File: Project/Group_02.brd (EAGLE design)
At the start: 71.1 x 44.5 mm, 29 parts, among them J1 POWER_JACKPTH_LOCK, U1 +12v

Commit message: Completamento board
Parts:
- moved C2 0.63 mm to (5.08, 38.7)
- moved C3 0.33 mm to (5.08, 35.2)
- moved J3 0.06 mm to (51.5, 31.1)
- moved J4 0.06 mm to (51.5, 36.7)
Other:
- board text added: "0.1μF"
- board text added: "0.33μF"
- board text added: "10K"
- board text added: "5V"
- board text added: "BOARD"
- board text added: "CY8CKIT059-TARGET"
- board text added: "D1 BLUE"
- board text added: "GND"
- board text added: "GROUP 02"
- board text added: "MUX PINS"
- board text added: "POWER JACK CONNECTOR"
- board text added: "PTC"
- board text added: "S1"
- board text added: "TCA 9546A"
- board text added: "TMP"
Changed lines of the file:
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@@
 <dimension x1="-1.27" y1="0" x2="-1.27" y2="44.45" x3="-2.54" y3="22.225" textsize="1.778" layer="51"/>
 <dimension x1="0" y1="46.99" x2="71.12" y2="46.99" x3="35.56" y3="45.72" textsize="1.778" layer="51"/>
-<hole x="3.175" y="42.291" drill="2.5"/>
-<hole x="3.175" y="2.032" drill="2.5"/>
-<hole x="68.58" y="2.032" drill="2.5"/>
-<hole x="68.58" y="42.291" drill="2.5"/>
+<hole x="3.175" y="42.291" drill="3"/>
+<hole x="3.175" y="1.905" drill="3"/>
+<hole x="68.58" y="1.905" drill="3"/>
+<hole x="68.58" y="42.291" drill="3"/>
+<text x="54.483" y="8.382" size="1.016" layer="21">CY8CKIT059-TARGET</text>
+<text x="39.116" y="33.147" size="0.8128" layer="21">TCA
+9546A</text>
+<text x="68.961" y="30.607" size="0.8128" layer="21" rot="R90">POWER JACK
+CONNECTOR</text>
+<text x="5.588" y="0.889" size="0.8128" layer="21">D1 BLUE</text>
+<text x="5.207" y="27.813" size="0.8128" layer="21">GND</text>
+<text x="3.175" y="27.813" size="0.8128" layer="21">5V</text>
+<wire x1="8.89" y1="25.4" x2="8.89" y2="24.13" width="0.1524" layer="21"/>
+<wire x1="8.89" y1="24.13" x2="11.43" y2="24.13" width="0.1524" layer="21"/>
+<wire x1="11.43" y1="24.13" x2="13.97" y2="24.13" width="0.1524" layer="21"/>
+<wire x1="13.97" y1="24.13" x2="16.51" y2="24.13" width="0.1524" layer="21"/>
+<wire x1="16.51" y1="24.13" x2="16.51" y2="25.4" width="0.1524" layer="21"/>
+<text x="9.906" y="22.86" size="0.8128" layer="21">MUX PINS</text>
+<wire x1="11.43" y1="25.4" x2="11.43" y2="24.13" width="0.1524" layer="21"/>
+<wire x1="13.97" y1="25.4" x2="13.97" y2="24.13" width="0.1524" layer="21"/>
+<text x="63.627" y="4.318" size="0.8128" layer="21">GND</text>
+<text x="66.802" y="4.318" size="0.8128" layer="21">5V</text>
+<text x="36.703" y="39.497" size="0.6096" layer="21">0.33μF</text>
+<text x="2.032" y="37.719" size="0.6096" layer="21" rot="R90">0.1μF</text>
+<text x="2.032" y="34.29" size="0.6096" layer="21" rot="R90">0.1μF</text>
+<text x="11.557" y="37.338" size="0.6096" layer="21">PTC</text>
+<text x="25.146" y="38.608" size="0.8128" layer="21">TMP</text>
+<text x="13.462" y="42.037" size="1.016" layer="21">S1</text>
+<text x="24.257" y="1.27" size="0.6096" layer="21">10K</text>
+<text x="57.15" y="42.164" size="1.27" layer="21">GROUP 02</text>
+<text x="59.69" y="40.513" size="1.27" layer="21">BOARD</text>
 </plain>
 <attributes>
@@
 <attribute name="VALUE" x="37.211" y="39.751" size="0.6096" layer="27" font="vector" ratio="20" rot="R270" align="top-center"/>
 </element>
-<element name="C2" library="SparkFun-Capacitors" package="CAP-PTH-SMALL-KIT" value="0.1uF" x="5.08" y="39.37" smashed="yes" rot="R180">
-<attribute name="PROD_ID" value="CAP-08370" x="-34.29" y="95.25" size="1.778" layer="27" rot="R180" display="off"/>
-</element>
-<element name="C3" library="SparkFun-Capacitors" package="CAP-PTH-SMALL-KIT" value="0.1uF" x="5.08" y="35.56" smashed="yes" rot="R180">
-<attribute name="PROD_ID" value="CAP-08370" x="-40.64" y="91.44" size="1.778" layer="27" rot="R180" display="off"/>
+<element name="C2" library="SparkFun-Capacitors" package="CAP-PTH-SMALL-KIT" value="0.1uF" x="5.08" y="38.735" smashed="yes" rot="R180">
+<attribute name="PROD_ID" value="CAP-08370" x="-34.29" y="94.615" size="1.778" layer="27" rot="R180" display="off"/>
+</element>
+<element name="C3" library="SparkFun-Capacitors" package="CAP-PTH-SMALL-KIT" value="0.1uF" x="5.08" y="35.2298" smashed="yes" rot="R180">
+<attribute name="PROD_ID" value="CAP-08370" x="-40.64" y="91.1098" size="1.778" layer="27" rot="R180" display="off"/>
 </element>
 <element name="D1" library="SparkFun-LED" package="LED-1206" value="BLUE" x="7.62" y="2.54" smashed="yes">
@@
 <attribute name="VALUE" x="2.54" y="29.718" size="0.6096" layer="27" font="vector" ratio="20"/>
 </element>
-<element name="J3" library="SparkFun-Connectors" package="1X02" value="" x="51.562" y="31.115" smashed="yes" rot="R90">
-<attribute name="NAME" x="50.165" y="29.845" size="0.6096" layer="25" font="vector" ratio="20" rot="R90"/>
-<attribute name="VALUE" x="53.594" y="29.845" size="0.6096" layer="27" font="vector" ratio="20" rot="R90"/>
-</element>
-<element name="J4" library="SparkFun-Connectors" package="1X02" value="" x="51.435" y="36.703" smashed="yes" rot="R90">
-<attribute name="NAME" x="50.038" y="35.433" size="0.6096" layer="25" font="vector" ratio="20" rot="R90"/>
-<attribute name="VALUE" x="53.467" y="35.433" size="0.6096" layer="27" font="vector" ratio="20" rot="R90"/>
+<element name="J3" library="SparkFun-Connectors" package="1X02" value="" x="51.4985" y="31.115" smashed="yes" rot="R90">
+<attribute name="NAME" x="50.1015" y="29.845" size="0.6096" layer="25" font="vector" ratio="20" rot="R90"/>
+<attribute name="VALUE" x="53.5305" y="29.845" size="0.6096" layer="27" font="vector" ratio="20" rot="R90"/>
+</element>
+<element name="J4" library="SparkFun-Connectors" package="1X02" value="" x="51.4985" y="36.703" smashed="yes" rot="R90">
+<attribute name="NAME" x="50.1015" y="35.433" size="0.6096" layer="25" font="vector" ratio="20" rot="R90"/>
+<attribute name="VALUE" x="53.5305" y="35.433" size="0.6096" layer="27" font="vector" ratio="20" rot="R90"/>
 </element>
 <element name="J5" library="SparkFun-Connectors" package="1X02" value="" x="33.655" y="38.862" smashed="yes" rot="R180">
@@
 <contactref element="U$1" pad="28"/>
 <contactref element="R11" pad="P$1"/>
-<contactref element="C3" pad="2"/>
-<contactref element="U$3" pad="12"/>
-<contactref element="U$2" pad="8"/>
 <contactref element="U$2" pad="3"/>
 <polygon width="0.2032" layer="1" isolate="0.3048">
@@
 <wire x1="24.892" y1="36.703" x2="24.257" y2="36.703" width="0.254" layer="1"/>
 <wire x1="24.257" y1="36.703" x2="22.86" y2="38.1" width="0.254" layer="1"/>
-<wire x1="22.86" y1="38.1" x2="21.409" y2="38.1" width="0.254" layer="1"/>
-<wire x1="21.409" y1="38.1" x2="20.104" y2="36.795" width="0.254" layer="1"/>
+<wire x1="22.86" y1="38.1" x2="21.59" y2="38.1" width="0.254" layer="1"/>
+<contactref element="U$3" pad="12"/>
+<contactref element="C3" pad="2"/>
+<contactref element="U$2" pad="8"/>
+<wire x1="21.59" y1="38.1" x2="21.409" y2="38.1" width="0.254" layer="1"/>
+<wire x1="20.104" y1="36.795" x2="21.409" y2="38.1" width="0.254" layer="1"/>
 </signal>
 <signal name="12V">
@@
 <via x="46.609" y="34.036" extent="1-16" drill="0.35"/>
 <wire x1="46.609" y1="34.036" x2="49.276" y2="36.703" width="0.254" layer="16"/>
-<wire x1="49.276" y1="36.703" x2="51.435" y2="36.703" width="0.254" layer="16"/>
+<wire x1="49.276" y1="36.703" x2="51.4985" y2="36.703" width="0.254" layer="16"/>
 <wire x1="44.95013125" y1="34.6938" x2="45.47386875" y2="34.6938" width="0.254" layer="1"/>
 <wire x1="45.47386875" y1="34.6938" x2="45.8442" y2="34.32346875" width="0.254" layer="1"/>
@@
 <contactref element="U$2" pad="7"/>
 <contactref element="R3" pad="1"/>
-<wire x1="51.435" y1="39.243" x2="48.983" y2="36.791" width="0.254" layer="1"/>
-<wire x1="48.983" y1="36.791" x2="48.983" y2="35.56" width="0.254" layer="1"/>
+<wire x1="51.4985" y1="39.243" x2="48.983" y2="36.7275" width="0.254" layer="1"/>
+<wire x1="48.983" y1="36.7275" x2="48.983" y2="35.56" width="0.254" layer="1"/>
 <wire x1="48.983" y1="35.56" x2="48.8192125" y2="35.56" width="0.254" layer="1"/>
 <wire x1="48.8192125" y1="35.56" x2="47.9382125" y2="36.441" width="0.254" layer="1"/>
@@
 <wire x1="43.54" y1="32.695" x2="44.45" y2="32.695" width="0.254" layer="1"/>
 <wire x1="49.149" y1="32.981" x2="51.015" y2="31.115" width="0.254" layer="1"/>
-<wire x1="51.015" y1="31.115" x2="51.562" y2="31.115" width="0.254" layer="1"/>
+<wire x1="51.015" y1="31.115" x2="51.4985" y2="31.115" width="0.254" layer="1"/>
 <wire x1="44.45" y1="32.695" x2="44.56086875" y2="32.695" width="0.254" layer="1"/>
 <wire x1="44.56086875" y1="32.695" x2="45.10426875" y2="32.1516" width="0.254" layer="1"/>
@@
 <wire x1="47.498" y1="34.04106875" x2="47.498" y2="32.981" width="0.254" layer="1"/>
 <wire x1="49.7542125" y1="33.912" x2="50.0112125" y2="33.655" width="0.254" layer="1"/>
-<wire x1="50.0112125" y1="33.655" x2="51.562" y2="33.655" width="0.254" layer="1"/>
+<wire x1="50.0112125" y1="33.655" x2="51.4985" y2="33.655" width="0.254" layer="1"/>
 <wire x1="47.498" y1="32.981" x2="48.429" y2="33.912" width="0.254" layer="1"/>
 <wire x1="48.429" y1="33.912" x2="49.7542125" y2="33.912" width="0.254" layer="1"/>
@@
 </board>
 </drawing>
+<compatibility>
+<note version="6.3" minversion="6.2.2" severity="warning">
+Since Version 6.2.2 text objects can contain more than one line,
+which will not be processed correctly with this version.
+</note>
+</compatibility>
 </eagle>

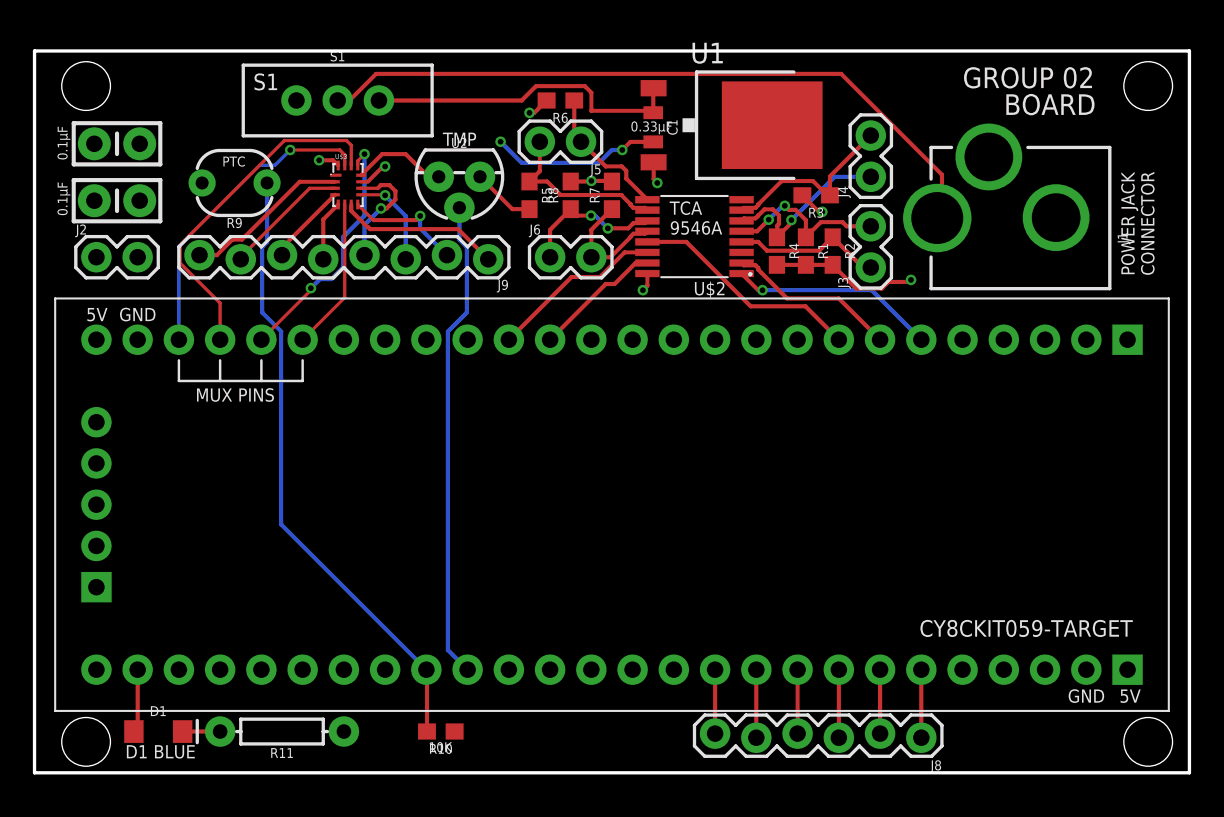
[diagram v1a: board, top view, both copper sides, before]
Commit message: Ottimizzazione dimensioni board
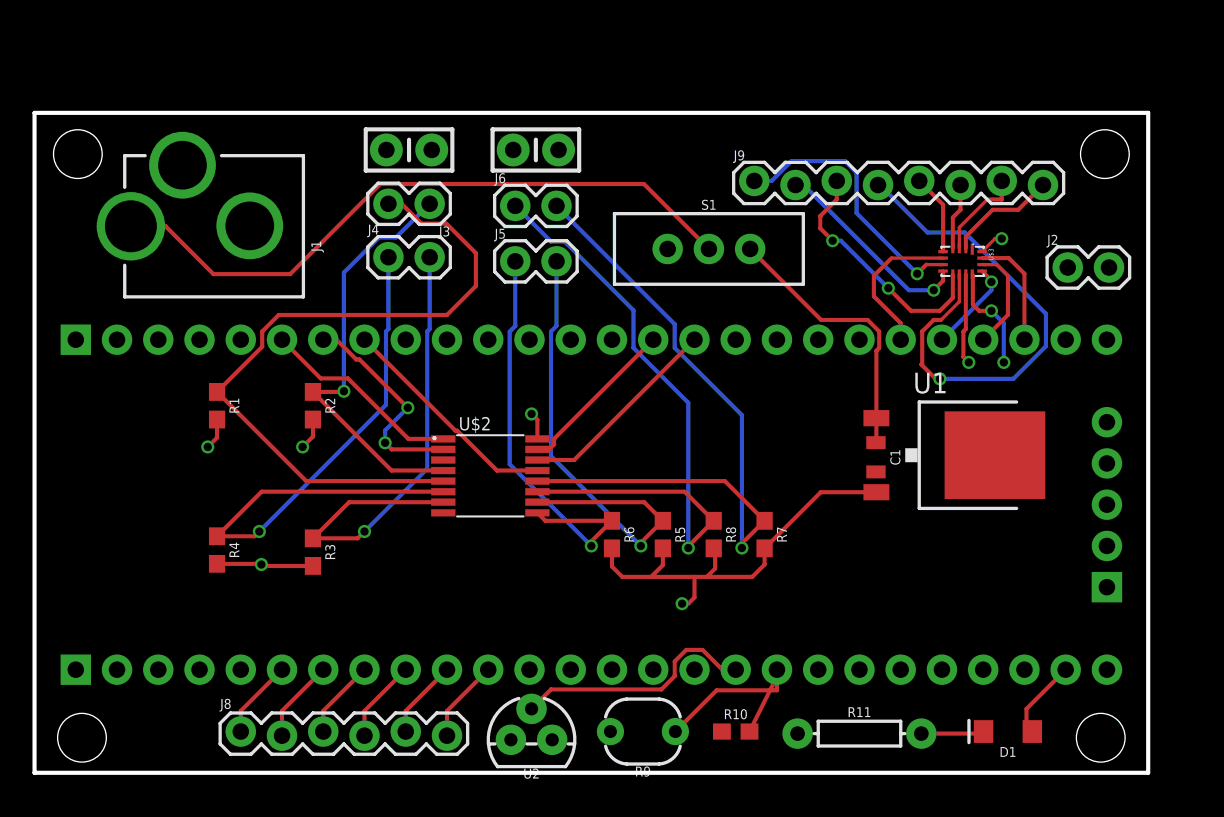
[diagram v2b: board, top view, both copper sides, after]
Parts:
- moved J2 59.8 mm to (63.6, 31.1)
- moved D1 52.3 mm to (59.9, 2.54), turned to 180 degrees
- moved J1 49.7 mm to (19.8, 33.7)
- moved R9 42.1 mm to (37.5, 2.54)
- moved J8 41.9 mm to (12.7, 2.54), turned to 0 degrees
- moved R4 39.1 mm to (11.2, 13.7)
- moved U$3 38.1 mm to (57.1, 31.5), turned to 270 degrees
- moved R3 38.0 mm to (17.1, 13.6), turned to 270 degrees
- moved R1 37.5 mm to (11.2, 22.6)
- moved R11 35.6 mm to (50.8, 2.41), turned to 0 degrees
- moved U2 35.0 mm to (30.6, 2.03), turned to 0 degrees
- moved R2 33.4 mm to (17.1, 22.6)
- moved J4 30.1 mm to (21.8, 31.8), turned to 0 degrees
- moved J3 27.4 mm to (24.3, 35.0), turned to 180 degrees
- moved R6 26.9 mm to (35.6, 14.7), turned to 270 degrees
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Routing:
- net I2C_SCL_3: track 7.62 -> 43.1 mm, vias 0 -> 1
- net I2C_SCL_0: track 10.5 -> 44.1 mm, vias 2 -> 0
- net I2C_SDA_3: track 8.89 -> 39.9 mm, vias 2 -> 1
- net I2C_SDA_1: track 11.5 -> 38.0 mm
- net PHOTO_OUT: track 38.1 -> 12.4 mm
- net N$14: track 7.29 -> 31.3 mm
- net 5V: track 24.2 -> 45.3 mm, vias 8 -> 7
- net I2C_SCL_1: track 11.3 -> 30.8 mm, vias 0 -> 1
- net I2C_SCL_2: track 10.7 -> 30.3 mm, vias 0 -> 1
- net I2C_SDA_2: track 8.55 -> 26.6 mm, vias 0 -> 1
- net I2C_SDA_0: track 9.30 -> 26.3 mm, vias 0 -> 1
- net MUX_A1: track 21.4 -> 6.45 mm
- net TEMP_OUT: track 29.6 -> 15.1 mm
- net MUX_A0: track 19.2 -> 7.07 mm, vias 1 -> 0
- net GND: track 16.4 -> 6.67 mm
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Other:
- board size 71.1 x 44.5 mm -> 68.6 x 40.6 mm
- board text removed: "0.1μF"
- board text removed: "0.33μF"
- board text removed: "10K"
- board text removed: "5V"
- board text removed: "BOARD"
- board text removed: "CY8CKIT059-TARGET"
- board text removed: "D1 BLUE"
- board text removed: "GND"
- board text removed: "GROUP 02"
- board text removed: "MUX PINS"
- board text removed: "POWER JACK CONNECTOR"
- board text removed: "PTC"
- board text removed: "S1"
- board text removed: "TCA 9546A"
- board text removed: "TMP"

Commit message: Completamento board super ridotta
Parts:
- moved C1 3.45 mm to (52.2, 16.0)
- moved U1 3.45 mm to (57.0, 16.1)
- moved J8 1.40 mm to (11.3, 2.54)
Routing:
- net GND: track 6.67 -> 11.4 mm
- net 12V: track 17.0 -> 20.4 mm
- net N$1: track 40.8 -> 38.3 mm
- net N$14: track 31.3 -> 32.5 mm
- net N$4: track 4.86 -> 5.52 mm
- net N$2: track 4.86 -> 5.52 mm
- net N$6: track 4.86 -> 5.52 mm
- net N$5: track 5.12 -> 5.69 mm
- net N$3: track 5.12 -> 5.69 mm
- net N$7: track 5.12 -> 5.69 mm
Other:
- board text added: "0.1μF"
- board text added: "0.33μf"
- board text added: "10K"
- board text added: "12V"
- board text added: "5V"
- board text added: "CY8CKIT059-TARGET"
- board text added: "D1 BLUE"
- board text added: "GND"
- board text added: "GROUP 02 BOARD"
- board text added: "MUX PINS"
- board text added: "POWER JACK CONNECTOR"
- board text added: "PTC"
- board text added: "S1"
- board text added: "TCA 9546A"
- board text added: "TMP"
- board text added: "V REG"

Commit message: Progetto board super ridotta
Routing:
- net N$14: track 32.5 -> 0.13 mm, vias 1 -> 0
- net N$17: track 16.7 -> 0.00 mm, vias 1 -> 0
- net N$15: track 15.4 -> 0.00 mm, vias 2 -> 0
- net N$16: track 12.6 -> 0.00 mm, vias 1 -> 0
- net MUX_OUT: track 9.33 -> 0.00 mm
- net MUX_A2: track 5.73 -> 0.00 mm, vias 1 -> 0
- net 5V: track 45.8 -> 44.3 mm, vias 7 -> 6
- removed copper zone on layer 16, net 5V
- removed copper zone on layer 1, net GND
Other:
- board outline removed
- board text removed: "0.1μF"
- board text removed: "0.33μf"
- board text removed: "10K"
- board text removed: "12V"
- board text removed: "5V"
- board text removed: "CY8CKIT059-TARGET"
- board text removed: "D1 BLUE"
- board text removed: "GND"
- board text removed: "GROUP 02 BOARD"
- board text removed: "MUX PINS"
- board text removed: "POWER JACK CONNECTOR"
- board text removed: "PTC"
- board text removed: "S1"
- board text removed: "TCA 9546A"
- board text removed: "TMP"
- board text removed: "V REG"

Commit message: Piccole modifiche e spostamenti
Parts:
- moved J4 1.65 mm to (23.3, 31.1)
- moved R3 1.63 mm to (18.4, 14.6)
- moved R4 1.63 mm to (12.5, 14.7)
- moved C2 1.57 mm to (24.6, 38.0)
- moved C3 1.57 mm to (32.4, 38.0)
- moved J5 1.57 mm to (31.1, 31.1)
- moved J3 1.57 mm to (25.9, 34.7)
- moved J6 1.55 mm to (31.1, 34.7)
- moved J8 1.37 mm to (12.6, 2.03)
- moved U2 1.28 mm to (31.9, 2.16)
- moved R9 1.27 mm to (38.7, 2.51)
- moved J2 1.27 mm to (64.9, 31.1)
- moved J9 1.27 mm to (45.6, 36.3)
- moved R10 1.27 mm to (44.5, 2.54)
- moved R11 1.27 mm to (52.1, 2.41)
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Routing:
- net N$14: track 0.13 -> 32.5 mm, vias 0 -> 1
- net N$17: track 0.00 -> 16.7 mm, vias 0 -> 1
- net N$15: track 0.00 -> 15.4 mm, vias 0 -> 2
- net N$16: track 0.00 -> 12.6 mm, vias 0 -> 1
- net MUX_OUT: track 0.00 -> 9.33 mm
- net MUX_A2: track 0.00 -> 5.73 mm, vias 0 -> 1
- net I2C_SDA_1: track 38.0 -> 36.0 mm
- net 5V: track 44.3 -> 45.8 mm, vias 6 -> 7
- net N$1: track 38.3 -> 39.2 mm
- net I2C_SCL_1: track 30.8 -> 30.0 mm
- net N$7: track 5.69 -> 6.20 mm
- net N$3: track 5.69 -> 6.20 mm
- net N$5: track 5.69 -> 6.20 mm
- added copper zone on layer 16, net 5V
- added copper zone on layer 1, net GND
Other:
- board outline added: 71.1 x 40.6 mm
- board text added: "0.1μF"
- board text added: "0.33μf"
- board text added: "10K"
- board text added: "12V"
- board text added: "5V"
- board text added: "CY8CKIT059-TARGET"
- board text added: "D1 BLUE"
- board text added: "GND"
- board text added: "GROUP 02 BOARD"
- board text added: "MUX PINS"
- board text added: "POWER JACK CONNECTOR"
- board text added: "PTC"
- board text added: "S1"
- board text added: "TCA 9546A"
- board text added: "TMP"
- board text added: "V REG"
